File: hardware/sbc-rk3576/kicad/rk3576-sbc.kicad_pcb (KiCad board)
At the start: 8 copper layers, 85 x 56 mm, 414 parts, among them J1001 USB3.0 A, J101 USB-C PWR/OTG, J501 DEBUG UART, J701 microSD, J801 M.2 M-KEY, J901 HDMI, Q901 BSS138, Q902 BSS138, Q903 BSS138, Q904 BSS138, Q905 BSS138, Q906 BSS138, Q907 BSS138, SW501 MASKROM, SW502 POWER, SW503 RESET, U1001 USBLC6-2SC6, U1002 TPD4E05U06, U1003 USBLC6-2SC6, U1004 AP2171W, U201 RK806S-5, U301 TPS562201, U302 TPS562201, U303 TPS562201, U304 TPS563201, U305 AP2171W, U401 RK3576, U601 LPDDR5 4GB, U701 eMMC 32GB, U702 AP2171W, U901 TPD4E05U06, U902 TPD4E05U06, Y501 24MHz

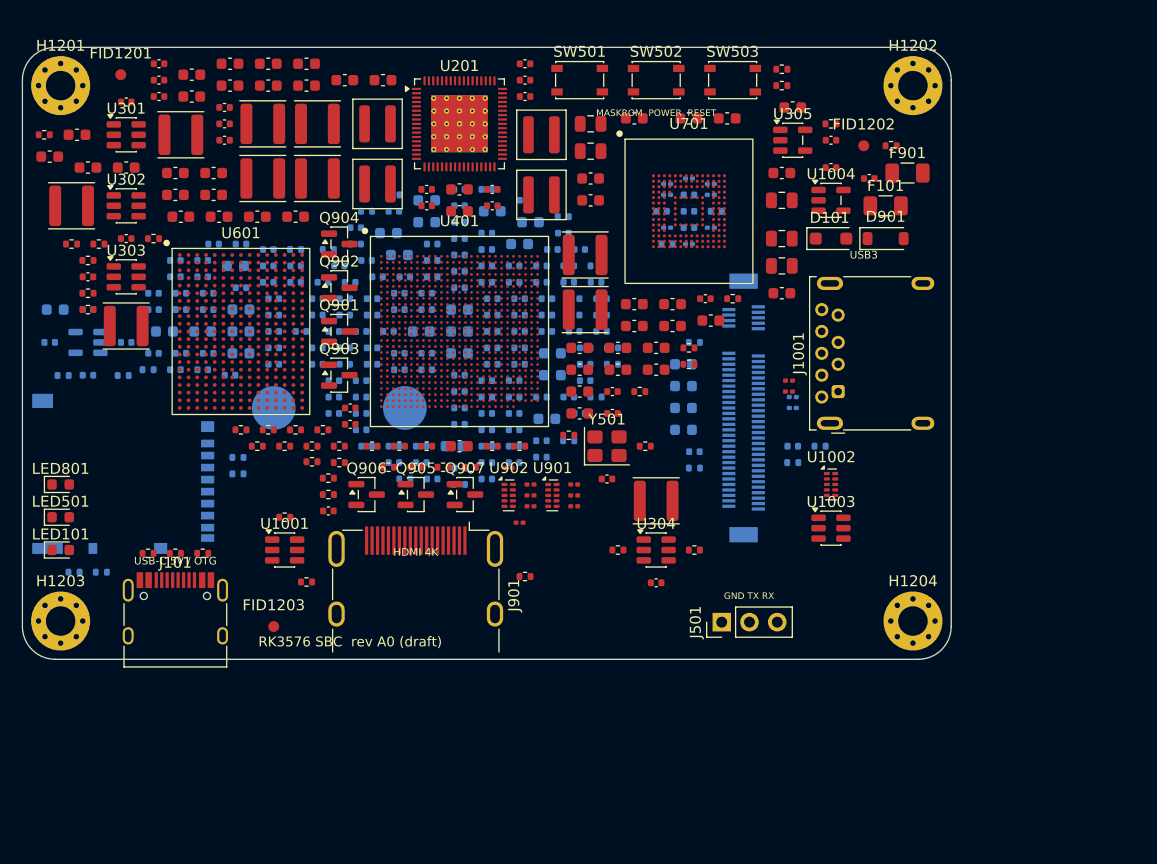
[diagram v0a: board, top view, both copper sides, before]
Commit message: hardware: add GbE, USB hub + 2x USB-A, Wi-Fi5/BT; real RK3576 land pattern; 100x72 board
- RK3576 footprint from LCSC C42388007 (all 698 ball IDs verified against the
  datasheet) replaces the placeholder.
- RTL8211F-CG RGMII PHY + HR911130C MagJack, FE1.1s 4-port hub (pinout per
  Terminus datasheet), stacked dual USB-A, BL-M8821CU1 Wi-Fi 5/BT 4.2 + u.FL.
- LCSC footprints get pad-derived courtyards; RJ45 pegs become NPTH.
- ERC 0/0, DRC 0 violations, parity 0 (placement stage).

Co-Authored-By: Claude Opus 5.5 <noreply@anthropic.com>
Claude-Session: https://claude.ai/code/session_01DP7VBm9fUdwhcDWq3gWKJ6
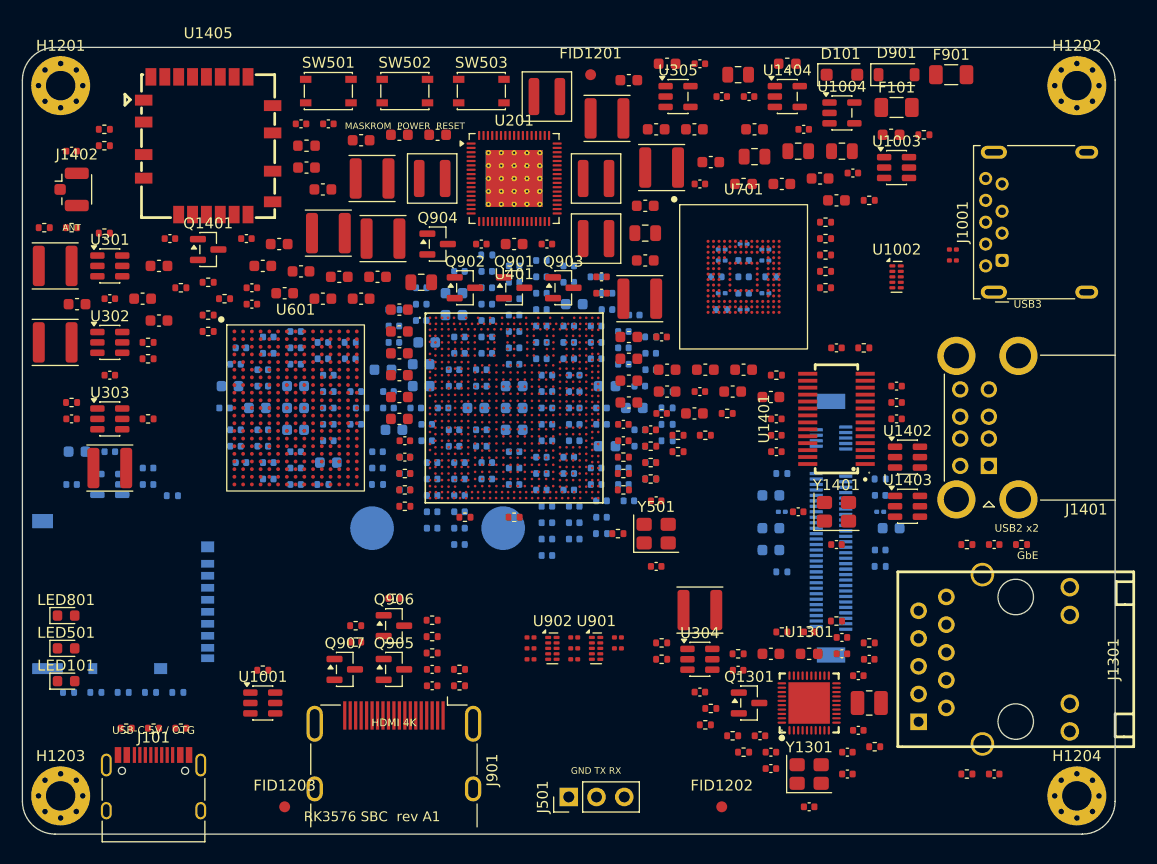
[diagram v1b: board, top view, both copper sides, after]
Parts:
- added C1301: 10uF, Capacitor_SMD:C_0603_1608Metric, F.Cu at (68.5, 55.5)
- added C1302: 100nF, Capacitor_SMD:C_0402_1005Metric, F.Cu at (76.5, 57.5)
- added C1303: 100nF, Capacitor_SMD:C_0402_1005Metric, F.Cu at (76.5, 62.5)
- added C1304: 100nF, Capacitor_SMD:C_0402_1005Metric, F.Cu at (75.0, 55.5)
- added C1305: 4.7uF, Capacitor_SMD:C_0402_1005Metric, F.Cu at (67.5, 63.0)
- added C1306: 4.7uF, Capacitor_SMD:C_0402_1005Metric, F.Cu at (68.5, 64.5)
- added C1307: 100nF, Capacitor_SMD:C_0402_1005Metric, F.Cu at (75.5, 64.5)
- added C1308: 100nF, Capacitor_SMD:C_0402_1005Metric, F.Cu at (72.0, 53.5)
- added C1309: 100nF, Capacitor_SMD:C_0402_1005Metric, F.Cu at (75.0, 54.0)
- added C1310: 100nF, Capacitor_SMD:C_0402_1005Metric, F.Cu at (77.5, 56.0)
- added C1311: 1uF, Capacitor_SMD:C_0402_1005Metric, F.Cu at (68.5, 66.0)
- added C1312: 15pF, Capacitor_SMD:C_0402_1005Metric, F.Cu at (72.0, 69.5)
- added C1313: 15pF, Capacitor_SMD:C_0402_1005Metric, F.Cu at (75.5, 66.5)
- added C1314: 1uF, Capacitor_SMD:C_0402_1005Metric, F.Cu at (65.5, 57.0)
- added C1315: 100nF, Capacitor_SMD:C_0402_1005Metric, F.Cu at (88.9, 45.5)
- added C1316: 100nF, Capacitor_SMD:C_0402_1005Metric, F.Cu at (88.9, 66.5)
- added C1401: 4.7uF, Capacitor_SMD:C_0402_1005Metric, F.Cu at (69.0, 34.0)
- added C1402: 100nF, Capacitor_SMD:C_0402_1005Metric, F.Cu at (80.0, 34.0)
- added C1403: 10uF, Capacitor_SMD:C_0603_1608Metric, F.Cu at (68.5, 32.0)
- added C1404: 100nF, Capacitor_SMD:C_0402_1005Metric, F.Cu at (80.0, 32.5)
- added C1405: 100nF, Capacitor_SMD:C_0402_1005Metric, F.Cu at (69.0, 35.5)
- added C1406: 1uF, Capacitor_SMD:C_0402_1005Metric, F.Cu at (80.0, 31.0)
- added C1407: 100nF, Capacitor_SMD:C_0402_1005Metric, F.Cu at (69.0, 37.0)
- added C1408: 1uF, Capacitor_SMD:C_0402_1005Metric, F.Cu at (74.5, 27.5)
- added C1409: 22pF, Capacitor_SMD:C_0402_1005Metric, F.Cu at (74.5, 45.5)
- added C1410: 22pF, Capacitor_SMD:C_0402_1005Metric, F.Cu at (71.0, 42.5)
- added C1411: 47uF, Capacitor_SMD:C_0805_2012Metric, F.Cu at (67.0, 10.0)
- added C1412: 100nF, Capacitor_SMD:C_0402_1005Metric, F.Cu at (64.0, 4.50)
- added C1413: 22uF, Capacitor_SMD:C_0603_1608Metric, F.Cu at (26.0, 11.0)
- added C1414: 1uF, Capacitor_SMD:C_0402_1005Metric, F.Cu at (25.5, 7.00)
- added C1415: 100nF, Capacitor_SMD:C_0402_1005Metric, F.Cu at (13.5, 17.5)
- added C1416: DNP, Capacitor_SMD:C_0402_1005Metric, F.Cu at (20.5, 17.5)
- added C1417: DNP, Capacitor_SMD:C_0402_1005Metric, F.Cu at (4.50, 9.50)
- added FB1301: 120R@100MHz, Inductor_SMD:L_0603_1608Metric, F.Cu at (72.0, 55.5)
- added FB1401: 120R@100MHz, Inductor_SMD:L_0603_1608Metric, F.Cu at (70.0, 1.50)
- added FB1402: 120R@100MHz, Inductor_SMD:L_0603_1608Metric, F.Cu at (26.0, 9.00)
- added J1301: RJ45 GbE, sbc:RJ45_Hanrun_HR911130C_MagJack, F.Cu at (88.9, 56.0)
- added J1401: USB2.0 A x2, Connector_USB:USB_A_CUI_UJ2-ADH-TH_Horizontal_Stacked, F.Cu at (88.4, 38.3)
- added J1402: u.FL, Connector_Coaxial:U.FL_Hirose_U.FL-R-SMT-1_Vertical, F.Cu at (4.50, 13.0)
- added L1301: 2.2uH, Inductor_SMD:L_1008_2520Metric, F.Cu at (77.5, 60.0)
- added Q1301: BSS138, Package_TO_SOT_SMD:SOT-23, F.Cu at (66.5, 60.0)
- added Q1401: BSS138, Package_TO_SOT_SMD:SOT-23, F.Cu at (17.0, 18.5)
- added R1301: 22R, Resistor_SMD:R_0402_1005Metric, F.Cu at (69.5, 53.5)
- added R1302: 22R, Resistor_SMD:R_0402_1005Metric, F.Cu at (78.0, 64.0)
- added R1303: 2.49k, Resistor_SMD:R_0402_1005Metric, F.Cu at (66.0, 64.5)
- added R1304: 1.5k, Resistor_SMD:R_0402_1005Metric, F.Cu at (65.0, 63.0)
- added R1305: 10k, Resistor_SMD:R_0402_1005Metric, F.Cu at (63.0, 60.5)
- added R1306: 100k, Resistor_SMD:R_0402_1005Metric, F.Cu at (62.5, 62.0)
- added R1307: 4.7k, Resistor_SMD:R_0402_1005Metric, F.Cu at (77.5, 54.5)
- added R1308: 4.7k, Resistor_SMD:R_0402_1005Metric, F.Cu at (74.5, 52.5)
- added R1309: 4.7k, Resistor_SMD:R_0402_1005Metric, F.Cu at (65.5, 55.5)
- added R1310: 4.7k, Resistor_SMD:R_0402_1005Metric, F.Cu at (86.4, 45.5)
- added R1311: 510R, Resistor_SMD:R_0402_1005Metric, F.Cu at (91.4, 45.5)
- added R1312: 510R, Resistor_SMD:R_0402_1005Metric, F.Cu at (86.4, 66.5)
- added R1401: 2.7k, Resistor_SMD:R_0402_1005Metric, F.Cu at (69.0, 30.0)
- added R1402: 10k, Resistor_SMD:R_0402_1005Metric, F.Cu at (77.0, 27.5)
- added R1403: 10k, Resistor_SMD:R_0402_1005Metric, F.Cu at (73.5, 16.0)
- added R1404: 10k, Resistor_SMD:R_0402_1005Metric, F.Cu at (7.50, 9.00)
- added R1405: 10k, Resistor_SMD:R_0402_1005Metric, F.Cu at (7.50, 7.50)
- added R1406: 10k, Resistor_SMD:R_0402_1005Metric, F.Cu at (17.0, 21.5)
- added R1407: 100k, Resistor_SMD:R_0402_1005Metric, F.Cu at (14.5, 22.0)
- added R1408: 0R, Resistor_SMD:R_0402_1005Metric, F.Cu at (4.50, 16.5)
- added U1301: RTL8211F-CG, sbc:WQFN-40-1EP_5x5mm_P0.4mm, F.Cu at (72.0, 60.0)
- added U1401: FE1.1s, sbc:SSOP-28_3.9x9.9mm_P0.635mm, F.Cu at (74.5, 34.0)
- added U1402: USBLC6-2SC6, Package_TO_SOT_SMD:SOT-23-6, F.Cu at (81.0, 37.5)
- added U1403: USBLC6-2SC6, Package_TO_SOT_SMD:SOT-23-6, F.Cu at (81.0, 42.0)
- added U1404: AP2171W, Package_TO_SOT_SMD:SOT-23-5, F.Cu at (70.0, 4.50)
- added U1405: BL-M8821CU1, sbc:WiFi_Module_22P_13.0x12.2mm_P1.27mm, F.Cu at (17.0, 9.00)
- added Y1301: 25MHz, Crystal:Crystal_SMD_3225-4Pin_3.2x2.5mm, F.Cu at (72.0, 66.5)
- added Y1401: 12MHz, Crystal:Crystal_SMD_3225-4Pin_3.2x2.5mm, F.Cu at (74.5, 42.5)
- U401: footprint sbc:RK3576_FCCSP-698_16.1x17.2mm_PLACEHOLDER -> sbc:RK3576_FCCSP-698_16.1x17.2mm
- moved FID1202 61.9 mm to (64.0, 69.5)
- moved C251 56.1 mm to (57.5, 35.0)
- moved R207 49.9 mm to (57.5, 38.0)
- moved C226 48.8 mm to (55.5, 30.5)
- moved C232 48.5 mm to (59.0, 31.5)
- moved R214 47.8 mm to (73.5, 22.0)
- moved C246 47.2 mm to (58.5, 33.5)
- moved C245 46.6 mm to (55.0, 34.5)
- moved C230 46.5 mm to (55.5, 32.5)
- moved R213 44.5 mm to (73.5, 20.5)
- moved C244 43.8 mm to (62.0, 1.50)
- moved FID1201 43.0 mm to (52.0, 2.50)
- moved C308 41.1 mm to (73.0, 12.0)
- moved C218 40.9 mm to (55.5, 26.5)
- moved C249 39.9 mm to (35.0, 36.0)
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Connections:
- U401 pad 1A10: unconnected-(U401F-GPIO3_D2/VO_LCDC_D1-Pad1A10) -> RGMII_RXD3
- U401 pad 1A11: unconnected-(U401F-GPIO3_B1/VO_LCDC_D18-Pad1A11) -> RGMII_RXD1
- U401 pad 1A12: unconnected-(U401F-GPIO3_D1/VO_LCDC_D2-Pad1A12) -> RGMII_RXC
- U401 pad 1A24: unconnected-(U401D-GPIO1_D2/ETH1_MDC_M1-Pad1A24) -> WIFI_PD_GPIO
- U401 pad 1A7: unconnected-(U401F-GPIO3_A6/VO_LCDC_D21-Pad1A7) -> ETH_MDC
- U401 pad 1A8: unconnected-(U401F-GPIO3_C3/VO_LCDC_D8-Pad1A8) -> RGMII_TXD2
- U401 pad 1A9: unconnected-(U401F-GPIO3_B5/VO_LCDC_D14-Pad1A9) -> RGMII_TXD0
- U401 pad 1D22: unconnected-(U401D-GPIO1_D1/ETH1_RXCTL_M1-Pad1D22) -> PHY_INT_L
- U401 pad 2T4: USB3A_DP -> HUB_UP_DP
- U401 pad 2T5: USB3A_DM -> HUB_UP_DM
- U401 pad A11: unconnected-(U401F-GPIO3_B3/VO_LCDC_D16-PadA11) -> RGMII_TXCTL
- U401 pad A13: unconnected-(U401F-GPIO3_B2/VO_LCDC_D17-PadA13) -> RGMII_RXD0
- U401 pad A9: unconnected-(U401F-GPIO3_A5/VO_LCDC_D22-PadA9) -> ETH_MDIO
- U401 pad B10: unconnected-(U401F-GPIO3_B4/VO_LCDC_D15-PadB10) -> RGMII_TXD1
- U401 pad B11: unconnected-(U401F-GPIO3_B6/VO_LCDC_D13-PadB11) -> RGMII_TXC_SOC
- U401 pad B12: unconnected-(U401F-GPIO3_D3/VO_LCDC_D0-PadB12) -> RGMII_RXD2
- U401 pad B13: unconnected-(U401F-GPIO3_A7/VO_LCDC_D20-PadB13) -> RGMII_RXCTL
- U401 pad B9: unconnected-(U401F-GPIO3_C2/VO_LCDC_D9-PadB9) -> RGMII_TXD3
- U401 pad C29: unconnected-(U401D-GPIO1_D0/ETH1_RXD1_M1-PadC29) -> PHY_RST_GPIO
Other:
- board size 85 x 56 mm -> 100 x 72 mm
- board text added: "ANT"
- board text added: "GbE"
- board text added: "RK3576 SBC rev A1"
- board text added: "USB2 x2"
- board text removed: "RK3576 SBC rev A0 (draft)"
- board text removed: "U401 LAND PATTERN = PLACEHOLDER"

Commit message: hardware: fix RK806 rail map (verified vs mainline DTS); add board device tree + Linux PC report
- RK806S-5 dcdc1-10 / nldo1-5 -> rail assignments now match mainline
  rk3576-rock-4d.dts (same PMIC OTP + SoC); rev A0 had 12 wrong.
- software/rk3576-sbc.dts compiles against mainline rk3576.dtsi
  (tools/check_dts.sh); all 7 DT GPIOs cross-checked with design.py nets.
- docs/linux_pc_readiness.md, length_report.py, route.py (Freerouting).

Co-Authored-By: Claude Opus 5.5 <noreply@anthropic.com>
Claude-Session: https://claude.ai/code/session_01DP7VBm9fUdwhcDWq3gWKJ6
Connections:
- C212 pad 1: VDD_LOGIC_S0 -> VDD_CPU_LIT_S0
- C213 pad 1: VDD_LOGIC_S0 -> VDD_CPU_LIT_S0
- C214 pad 1: VDD_LOGIC_S0 -> VDD_CPU_LIT_S0
- C216 pad 1: VDD_GPU_S0 -> VCC_3V3_S3
- C217 pad 1: VDD_GPU_S0 -> VCC_3V3_S3
- C218 pad 1: VDD_GPU_S0 -> VCC_3V3_S3
- C220 pad 1: VDD_CPU_LIT_S0 -> VDD_GPU_S0
- C221 pad 1: VDD_CPU_LIT_S0 -> VDD_GPU_S0
- C223 pad 1: VDD_DDR_S0 -> VDDQ_DDR_S0
- C224 pad 1: VDD_DDR_S0 -> VDDQ_DDR_S0
- C226 pad 1: VCC_3V3_S3 -> VDD_LOGIC_S0
- C227 pad 1: VCC_3V3_S3 -> VDD_LOGIC_S0
- C229 pad 1: VDD2H_DDR_S3 -> VCC_1V8_S3
- C230 pad 1: VDD2H_DDR_S3 -> VCC_1V8_S3
- C232 pad 1: VCC_1V8_S3 -> VDD2H_DDR_S3
- C233 pad 1: VCC_1V8_S3 -> VDD2H_DDR_S3
- C235 pad 1: VDDQ_DDR_S0 -> VDD_DDR_S0
- C236 pad 1: VDDQ_DDR_S0 -> VDD_DDR_S0
- C237 pad 1: VDDA_DDR_PLL_S0 -> VDDA_0V75_S0
- C238 pad 1: VDDA0V75_HDMI_S0 -> VDDA_0V85_S0
- C239 pad 1: VDDA_0V75_S0 -> VDDA0V75_HDMI_S0
- C240 pad 1: VDDA_0V85_S0 -> VDDA_DDR_PLL_S0
- L203 pad 2: VDD_LOGIC_S0 -> VDD_CPU_LIT_S0
- L204 pad 2: VDD_GPU_S0 -> VCC_3V3_S3
- L205 pad 2: VDD_CPU_LIT_S0 -> VDD_GPU_S0
- L206 pad 2: VDD_DDR_S0 -> VDDQ_DDR_S0
- L207 pad 2: VCC_3V3_S3 -> VDD_LOGIC_S0
- L208 pad 2: VDD2H_DDR_S3 -> VCC_1V8_S3
- L209 pad 2: VCC_1V8_S3 -> VDD2H_DDR_S3
- L210 pad 2: VDDQ_DDR_S0 -> VDD_DDR_S0
- R205 pad 2: VDD_CPU_LIT_S0 -> VDD_GPU_S0
- R207 pad 2: VDD_DDR_S0 -> VDDQ_DDR_S0
- R209 pad 2: VCC_1V8_S3 -> VDD2H_DDR_S3
- U201 pad 10: VDDA0V75_HDMI_S0 -> VDDA_0V85_S0
- U201 pad 11: VDDA_0V75_S0 -> VDDA0V75_HDMI_S0
- U201 pad 12: VDDA_0V85_S0 -> VDDA_DDR_PLL_S0
- U201 pad 24: VDD_GPU_S0 -> VCC_3V3_S3
- U201 pad 25: VDDQ_DDR_S0 -> VDD_DDR_S0
- U201 pad 30: VDD_DDR_S0 -> VDDQ_DDR_S0
- U201 pad 41: VCC_3V3_S3 -> VDD_LOGIC_S0
- U201 pad 46: VDD_CPU_LIT_S0 -> VDD_GPU_S0
- U201 pad 5: VDD2H_DDR_S3 -> VCC_1V8_S3
- U201 pad 56: VDD_LOGIC_S0 -> VDD_CPU_LIT_S0
- U201 pad 67: VCC_1V8_S3 -> VDD2H_DDR_S3
- U201 pad 8: VDDA_DDR_PLL_S0 -> VDDA_0V75_S0

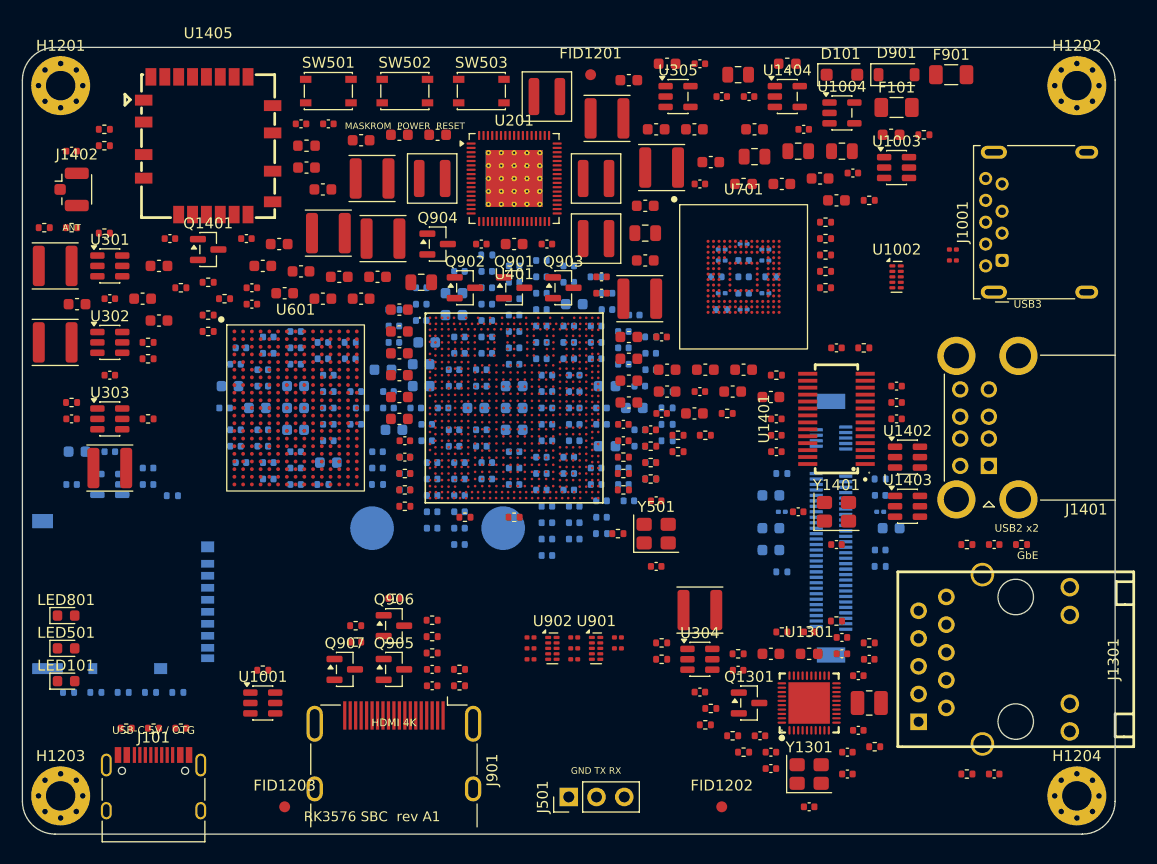
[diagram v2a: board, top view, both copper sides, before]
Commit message: hardware: BGA via-in-pad fan-out, chunked Freerouting, routing-safe build
- tools/fanout.py: 818 via-in-pad escapes (RK3576 0.25/0.15, LPDDR5 0.30/0.15);
  bottom side under the BGAs reserved for vias, decaps ring the BGAs.
- GND plane clearance 0.1 mm to keep webs in the 0.55 mm via field.
- route.py: job timeout + save per chunk, telemetry off, resumes from board.
- build.sh only re-places the PCB with REGEN_PCB=1; adds length report.
- Board state: fan-out + first test routing chunk (routing in progress).

Co-Authored-By: Claude Opus 5.5 <noreply@anthropic.com>
Claude-Session: https://claude.ai/code/session_01DP7VBm9fUdwhcDWq3gWKJ6
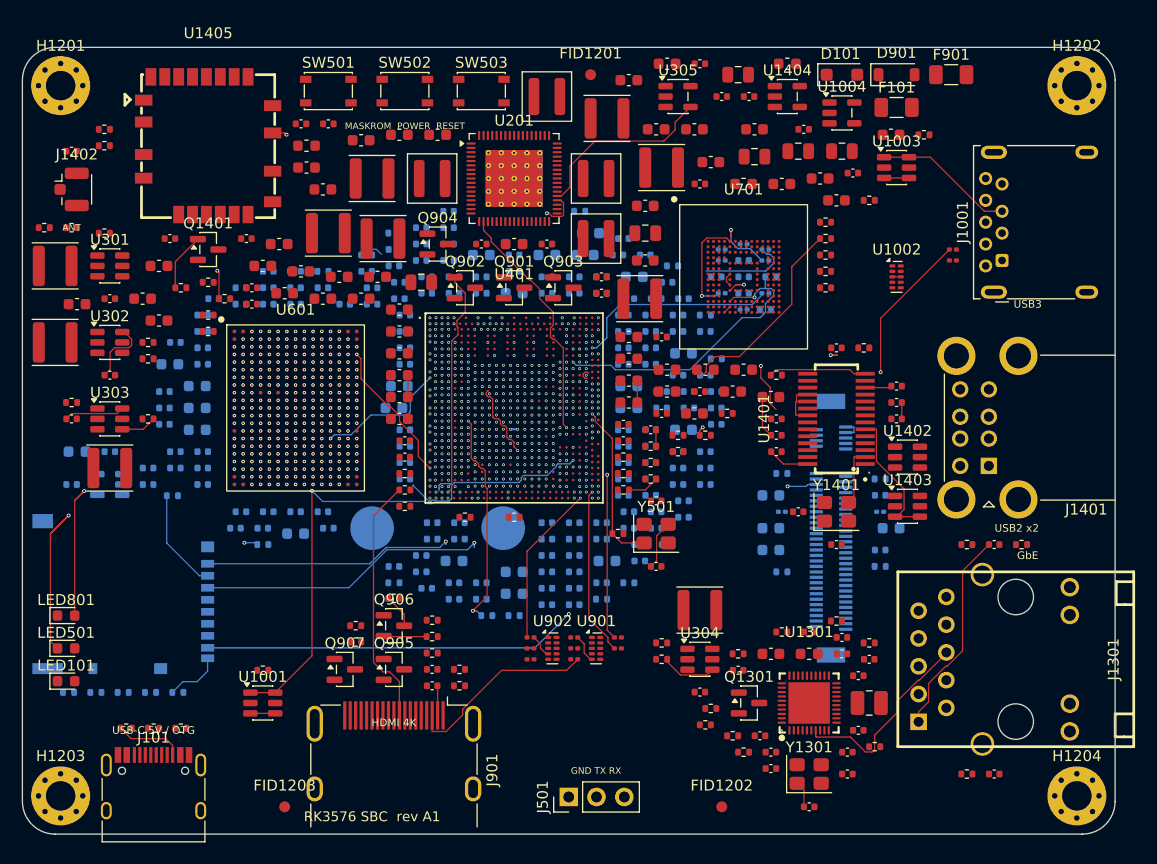
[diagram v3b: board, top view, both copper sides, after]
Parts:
- moved R916 33.6 mm to (59.5, 20.0)
- moved C498 32.2 mm to (50.5, 51.0)
- moved C495 31.8 mm to (63.5, 31.5)
- moved C494 31.4 mm to (36.5, 16.5)
- moved C484 31.1 mm to (48.0, 51.0)
- moved C482 31.0 mm to (34.0, 18.5)
- moved C478 30.2 mm to (62.5, 37.0)
- moved C480 30.0 mm to (56.5, 47.0)
- moved C483 29.6 mm to (34.0, 47.5)
- moved R505 29.6 mm to (42.5, 52.0)
- moved C476 28.9 mm to (42.0, 50.5)
- moved C466 28.7 mm to (32.0, 22.0)
- moved C473 28.4 mm to (39.0, 16.5)
- moved C459 28.0 mm to (45.0, 50.0)
- moved C462 27.9 mm to (54.5, 19.0)
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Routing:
- net SD_D1: track 0.00 -> 61.5 mm, vias 0 -> 2
- net SD_CMD: track 0.00 -> 52.1 mm, vias 0 -> 2
- net SD_D2: track 0.00 -> 49.6 mm, vias 0 -> 2
- net USB3_TXN: track 0.00 -> 40.4 mm, vias 0 -> 2
- net PMIC_FB2: track 0.00 -> 39.9 mm, vias 0 -> 2
- net LED_SYS_L: track 0.00 -> 37.5 mm, vias 0 -> 2
- net PCIE0_WAKE_L: track 0.00 -> 35.1 mm, vias 0 -> 2
- net DBG_UART_RX: track 0.00 -> 34.1 mm, vias 0 -> 1
- net DBG_UART_TX: track 0.00 -> 34.0 mm, vias 0 -> 1
- net USBC_DP: track 0.00 -> 33.7 mm, vias 0 -> 2
- net RGMII_RXD0: track 0.00 -> 30.1 mm, vias 0 -> 2
- net EMMC_CMD: track 0.00 -> 28.2 mm, vias 0 -> 2
- net LP5_DQ11_B: track 0.00 -> 25.3 mm, vias 0 -> 2
- net LP5_DMI0_A: track 0.00 -> 23.5 mm, vias 0 -> 2
- net HDMI_D0N_C: track 0.00 -> 23.0 mm
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
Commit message: hardware: routing chunk 1 + GND plane stitching (unrouted 1343 -> ~700)
- Freerouting chunk 1 imported (1343 -> 940 unrouted).
- tools/stitch.py: 284 GND stub+via plane connections with clearance,
  hole-spacing and keepout checks.
- hole clearance rule 0.12 mm (fine-pitch BGA fab class).

Co-Authored-By: Claude Opus 5.5 <noreply@anthropic.com>
Claude-Session: https://claude.ai/code/session_01DP7VBm9fUdwhcDWq3gWKJ6
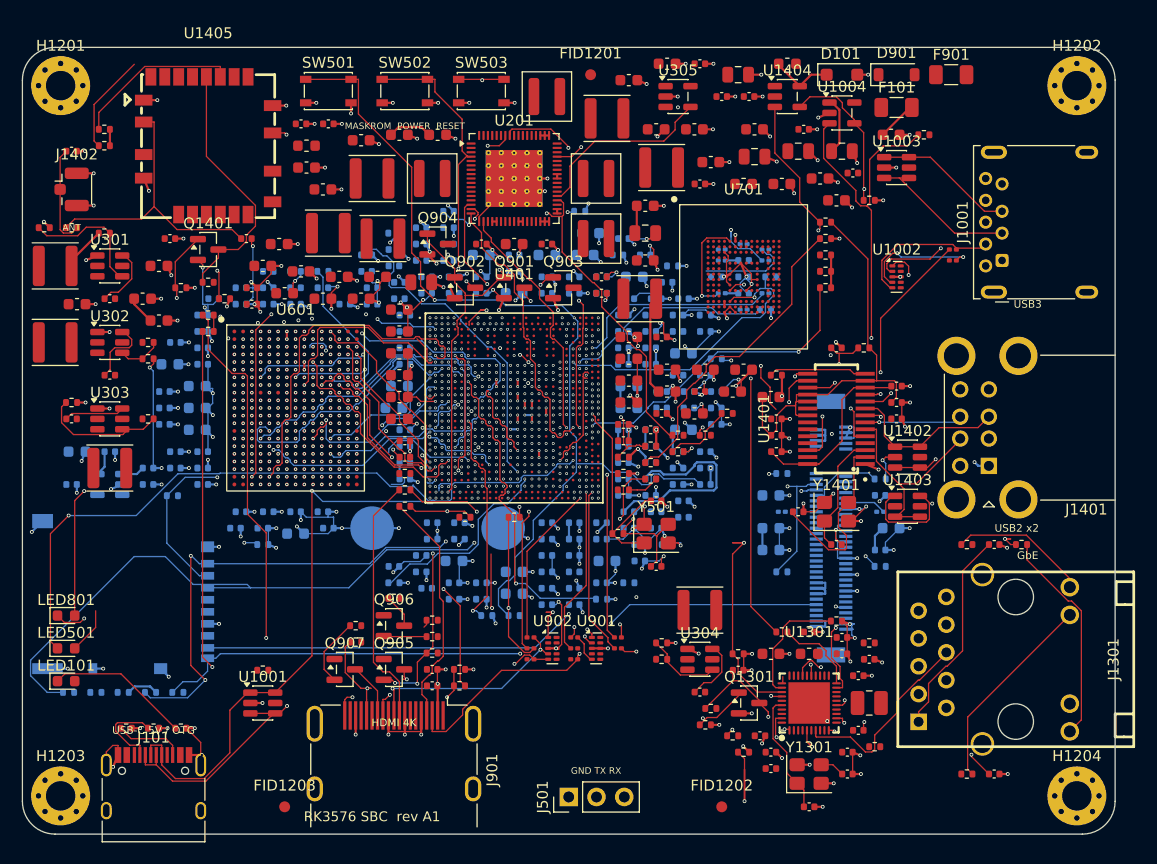
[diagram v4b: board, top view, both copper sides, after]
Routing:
- net GND: track 14.5 -> 513.9 mm, vias 370 -> 685
- net SARADC_IN0_BOOT: track 0.00 -> 86.1 mm, vias 1 -> 2
- net WIFI_USB_DP: track 1.97 -> 73.5 mm, vias 1 -> 2
- net M2_LED_L: track 0.00 -> 70.7 mm, vias 0 -> 2
- net HDMI_D3N_C: track 0.00 -> 66.8 mm, vias 0 -> 3
- net USB3A_OC_L: track 0.00 -> 64.9 mm, vias 1 -> 2
- net HDMI_D3P_C: track 2.14 -> 65.9 mm, vias 0 -> 3
- net M2_LED_A: track 14.2 -> 77.6 mm, vias 1 -> 2
- net RGMII_TXCTL: track 2.30 -> 65.5 mm, vias 2 -> 3
- net USB_HOST_PWREN: track 0.00 -> 62.2 mm, vias 1 -> 3
- net USB3_RXN: track 0.00 -> 51.5 mm, vias 1 -> 2
- net SD_DET_L: track 5.22 -> 55.8 mm, vias 1 -> 2
- net RGMII_TXC_SOC: track 0.00 -> 50.4 mm, vias 1 -> 2
- net RESET_KEY: track 0.00 -> 49.3 mm, vias 0 -> 3
- net PHY_LED1: track 0.00 -> 48.8 mm, vias 0 -> 2
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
